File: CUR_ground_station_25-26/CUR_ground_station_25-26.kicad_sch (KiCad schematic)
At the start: 0 parts

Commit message: added sheets and mcu
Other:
- added sheet MCU (MCU.kicad_sch)
- added sheet Power (Power.kicad_sch)
- added sheet Telemetry (Telemetry.kicad_sch)
- added sheet User Interface (Peripherals.kicad_sch)
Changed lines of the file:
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@@
 	(generator_version "9.0")
 	(paper "A4")
+	(sheet
+		(at 77.47 91.44)
+		(size 39.37 17.78)
+		(exclude_from_sim no)
+		(in_bom yes)
+		(on_board yes)
+		(dnp no)
+		(fields_autoplaced yes)
+		(stroke
+			(width 0.1524)
+			(type solid)
+		)
+		(fill
+			(color 0 0 0 0.0000)
+		)
+		(property "Sheetname" "User Interface"
+			(at 77.47 90.7284 0)
+			(effects
+				(font
+					(size 1.27 1.27)
+				)
+				(justify left bottom)
+			)
+		)
+		(property "Sheetfile" "Peripherals.kicad_sch"
+			(at 77.47 109.8046 0)
+			(effects
+				(font
+					(size 1.27 1.27)
+				)
+				(justify left top)
+			)
+		)
+		(instances
+			(project "CUR_ground_station_25-26"
+				(path "/b6f682bd-f29b-4650-adb4-b230be0368ad"
+					(page "5")
+				)
+			)
+		)
+	)
+	(sheet
+		(at 167.64 109.22)
+		(size 43.18 17.78)
+		(exclude_from_sim no)
+		(in_bom yes)
+		(on_board yes)
+		(dnp no)
+		(fields_autoplaced yes)
+		(stroke
+			(width 0.1524)
+			(type solid)
+		)
+		(fill
+			(color 0 0 0 0.0000)
+		)
+		(property "Sheetname" "Power"
+			(at 167.64 108.5084 0)
+			(effects
+				(font
+					(size 1.27 1.27)
+				)
+				(justify left bottom)
+			)
+		)
+		(property "Sheetfile" "Power.kicad_sch"
+			(at 167.64 127.5846 0)
+			(effects
+				(font
+					(size 1.27 1.27)
+				)
+				(justify left top)
+			)
+		)
+		(instances
+			(project "CUR_ground_station_25-26"
+				(path "/b6f682bd-f29b-4650-adb4-b230be0368ad"
+					(page "4")
+				)
+			)
+		)
+	)
+	(sheet
+		(at 124.46 66.04)
+		(size 36.83 78.74)
+		(exclude_from_sim no)
+		(in_bom yes)
+		(on_board yes)
+		(dnp no)
+		(fields_autoplaced yes)
+		(stroke
+			(width 0.1524)
+			(type solid)
+		)
+		(fill
+			(color 0 0 0 0.0000)
+		)
+		(property "Sheetname" "MCU"
+			(at 124.46 65.3284 0)
+			(effects
+				(font
+					(size 1.27 1.27)
+				)
+				(justify left bottom)
+			)
+		)
+		(property "Sheetfile" "MCU.kicad_sch"
+			(at 124.46 145.3646 0)
+			(effects
+				(font
+					(size 1.27 1.27)
+				)
+				(justify left top)
+			)
+		)
+		(instances
+			(project "CUR_ground_station_25-26"
+				(path "/b6f682bd-f29b-4650-adb4-b230be0368ad"
+					(page "2")
+				)
+			)
+		)
+	)
+	(sheet
+		(at 167.64 76.2)
+		(size 43.18 22.86)
+		(exclude_from_sim no)
+		(in_bom yes)
+		(on_board yes)
+		(dnp no)
+		(fields_autoplaced yes)
+		(stroke
+			(width 0.1524)
+			(type solid)
+		)
+		(fill
+			(color 0 0 0 0.0000)
+		)
+		(property "Sheetname" "Telemetry"
+			(at 167.64 75.4884 0)
+			(effects
+				(font
+					(size 1.27 1.27)
+				)
+				(justify left bottom)
+			)
+		)
+		(property "Sheetfile" "Telemetry.kicad_sch"
+			(at 167.64 99.6446 0)
+			(effects
+				(font
+					(size 1.27 1.27)
+				)
+				(justify left top)
+			)
+		)
+		(instances
+			(project "CUR_ground_station_25-26"
+				(path "/b6f682bd-f29b-4650-adb4-b230be0368ad"
+					(page "3")
+				)
+			)
+		)
+	)
 	(sheet_instances
 		(path "/"

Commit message: added user stuff
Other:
- sheet MCU ports: added BTN_1, BUZZER, LED_1_B, LED_1_G, LED_1_R, LED_2_B, LED_2_G, LED_2_R, LED_3_B, LED_3_G, LED_3_R; removed none
- sheet User Interface ports: added BTN_1, Buzzer, LED_1_B, LED_1_G, LED_1_R, LED_2_B, LED_2_G, LED_2_R, LED_3_B, LED_3_G, LED_3_R; removed none

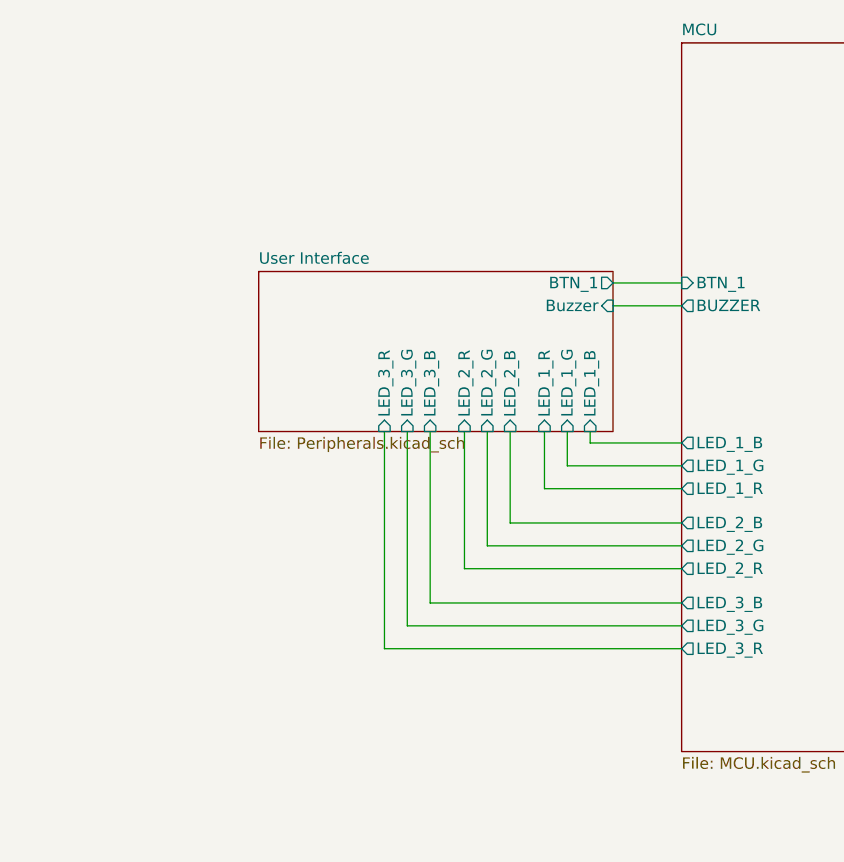
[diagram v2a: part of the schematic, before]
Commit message: Add some required MCU components
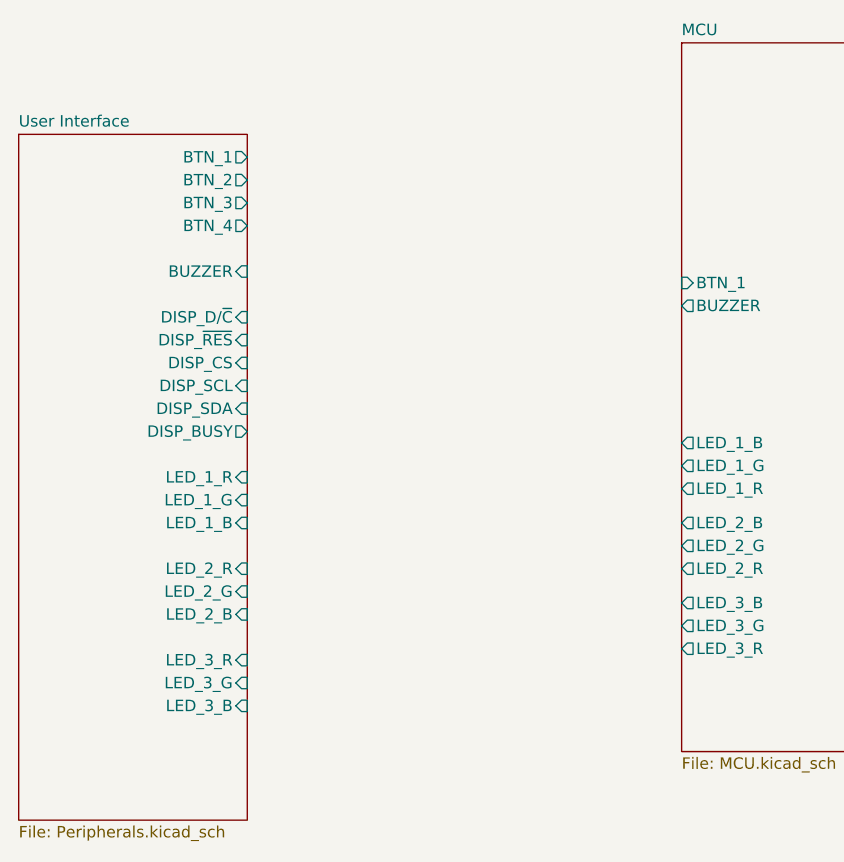
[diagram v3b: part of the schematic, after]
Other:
- sheet User Interface ports: added BTN_2, BTN_3, BTN_4, BUZZER, DISP_BUSY, DISP_CS, DISP_D/~{C}, DISP_SCL, DISP_SDA, DISP_~{RES}; removed Buzzer

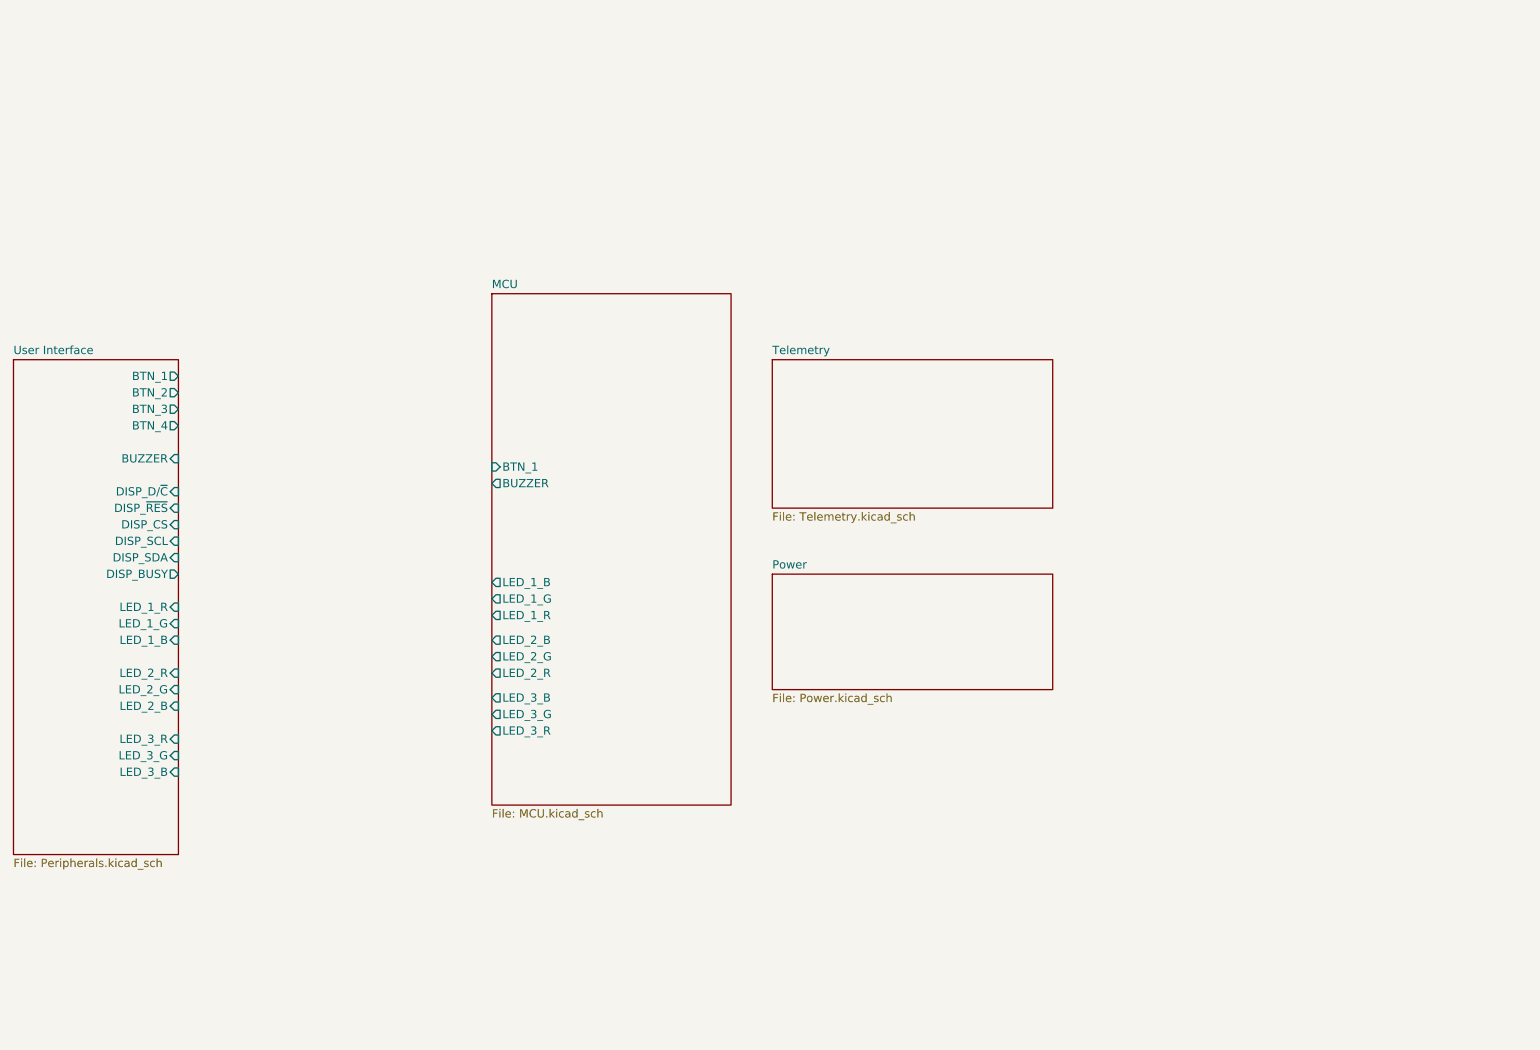
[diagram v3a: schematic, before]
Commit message: Sync sheet pins
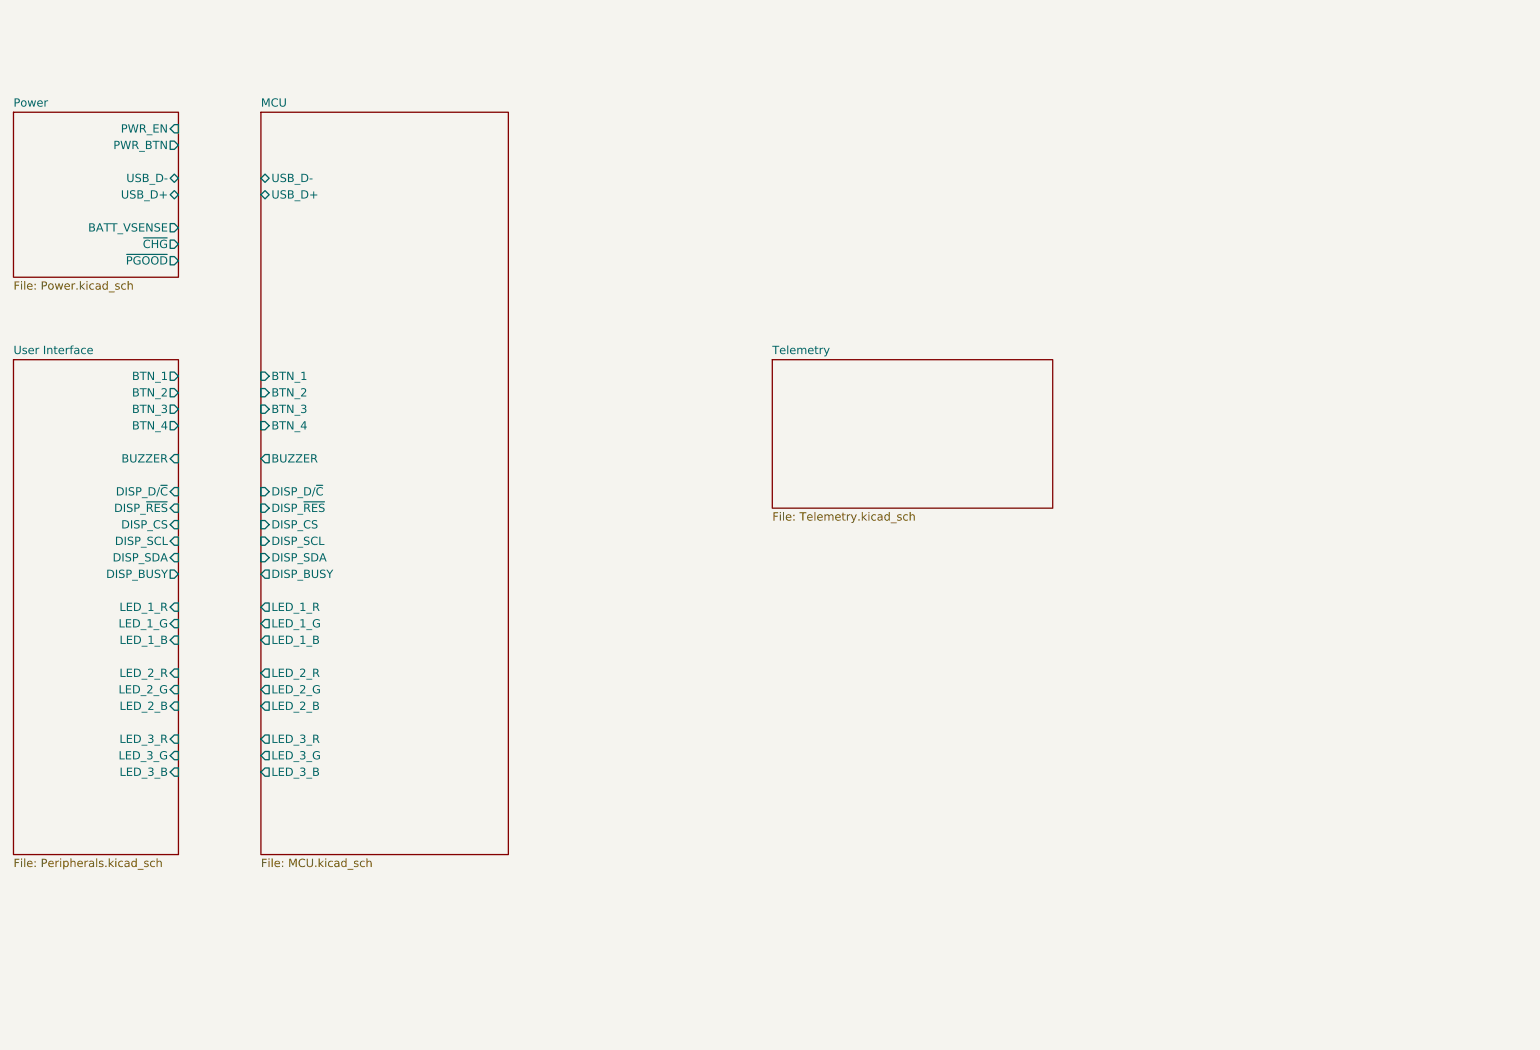
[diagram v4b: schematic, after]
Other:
- sheet MCU ports: added BTN_2, BTN_3, BTN_4, DISP_BUSY, DISP_CS, DISP_D/~{C}, DISP_SCL, DISP_SDA, DISP_~{RES}, USB_D+, USB_D-; removed none
- sheet Power ports: added BATT_VSENSE, PWR_BTN, PWR_EN, USB_D+, USB_D-, ~{CHG}, ~{PGOOD}; removed none
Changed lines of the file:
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@@
 	)
 	(sheet
-		(at 167.64 109.22)
-		(size 43.18 17.78)
+		(at 50.8 38.1)
+		(size 25.4 25.4)
 		(exclude_from_sim no)
 		(in_bom yes)
@@
 		)
 		(property "Sheetname" "Power"
-			(at 167.64 108.5084 0)
+			(at 50.8 37.3884 0)
 			(effects
 				(font
@@
 		)
 		(property "Sheetfile" "Power.kicad_sch"
-			(at 167.64 127.5846 0)
+			(at 50.8 64.0846 0)
 			(effects
 				(font
@@
 				)
 				(justify left top)
+			)
+		)
+		(pin "~{PGOOD}" output
+			(at 76.2 60.96 0)
+			(effects
+				(font
+					(size 1.27 1.27)
+				)
+				(justify right)
+			)
+		)
+		(pin "~{CHG}" output
+			(at 76.2 58.42 0)
+			(effects
+				(font
+					(size 1.27 1.27)
+				)
+				(justify right)
+			)
+		)
+		(pin "BATT_VSENSE" output
+			(at 76.2 55.88 0)
+			(effects
+				(font
+					(size 1.27 1.27)
+				)
+				(justify right)
+			)
+		)
+		(pin "PWR_EN" input
+			(at 76.2 40.64 0)
+			(effects
+				(font
+					(size 1.27 1.27)
+				)
+				(justify right)
+			)
+		)
+		(pin "USB_D-" bidirectional
+			(at 76.2 48.26 0)
+			(effects
+				(font
+					(size 1.27 1.27)
+				)
+				(justify right)
+			)
+		)
+		(pin "USB_D+" bidirectional
+			(at 76.2 50.8 0)
+			(effects
+				(font
+					(size 1.27 1.27)
+				)
+				(justify right)
+			)
+		)
+		(pin "PWR_BTN" output
+			(at 76.2 43.18 0)
+			(effects
+				(font
+					(size 1.27 1.27)
+				)
+				(justify right)
 			)
 		)
@@
 	)
 	(sheet
-		(at 124.46 66.04)
-		(size 36.83 78.74)
+		(at 88.9 38.1)
+		(size 38.1 114.3)
 		(exclude_from_sim no)
 		(in_bom yes)
@@
 		)
 		(property "Sheetname" "MCU"
-			(at 124.46 65.3284 0)
+			(at 88.9 37.3884 0)
 			(effects
 				(font
@@
 		)
 		(property "Sheetfile" "MCU.kicad_sch"
-			(at 124.46 145.3646 0)
+			(at 88.9 152.9846 0)
 			(effects
 				(font
@@
 		)
 		(pin "BTN_1" input
-			(at 124.46 92.71 180)
+			(at 88.9 78.74 180)
 			(effects
 				(font
@@
 		)
 		(pin "BUZZER" output
-			(at 124.46 95.25 180)
+			(at 88.9 91.44 180)
 			(effects
 				(font
@@
 		)
 		(pin "LED_1_B" output
-			(at 124.46 110.49 180)
+			(at 88.9 119.38 180)
 			(effects
 				(font
@@
 		)
 		(pin "LED_1_G" output
-			(at 124.46 113.03 180)
+			(at 88.9 116.84 180)
 			(effects
 				(font
@@
 		)
 		(pin "LED_1_R" output
-			(at 124.46 115.57 180)
+			(at 88.9 114.3 180)
 			(effects
 				(font
@@
 		)
 		(pin "LED_2_B" output
-			(at 124.46 119.38 180)
+			(at 88.9 129.54 180)
 			(effects
 				(font
@@
 		)
 		(pin "LED_2_G" output
-			(at 124.46 121.92 180)
+			(at 88.9 127 180)
 			(effects
 				(font
@@
 		)
 		(pin "LED_2_R" output
-			(at 124.46 124.46 180)
+			(at 88.9 124.46 180)
 			(effects
 				(font
@@
 		)
 		(pin "LED_3_B" output
-			(at 124.46 128.27 180)
+			(at 88.9 139.7 180)
 			(effects
 				(font
@@
 		)
 		(pin "LED_3_G" output
-			(at 124.46 130.81 180)
+			(at 88.9 137.16 180)
 			(effects
 				(font
@@
 		)
 		(pin "LED_3_R" output
-			(at 124.46 133.35 180)
-			(effects
-				(font
+			(at 88.9 134.62 180)
+			(effects
+				(font
+					(size 1.27 1.27)
+				)
+				(justify left)
+			)
+		)
+		(pin "BTN_4" input
+			(at 88.9 86.36 180)
+			(effects
+				(font
+					(size 1.27 1.27)
+				)
+				(justify left)
+			)
+		)
+		(pin "USB_D-" bidirectional
+			(at 88.9 48.26 180)
+			(effects
+				(font
+					(size 1.27 1.27)
+				)
+				(justify left)
+			)
+		)
+		(pin "DISP_D/~{C}" input
+			(at 88.9 96.52 180)
+			(effects
+				(font
+					(size 1.27 1.27)
+				)
+				(justify left)
+			)
+		)
+		(pin "DISP_CS" input
+			(at 88.9 101.6 180)
+			(effects
+				(font
+					(size 1.27 1.27)
+				)
+				(justify left)
+			)
+		)
+		(pin "DISP_SDA" input
+			(at 88.9 106.68 180)
+			(effects
+				(font
+					(size 1.27 1.27)
+				)
+				(justify left)
+			)
+		)
+		(pin "DISP_~{RES}" input
+			(at 88.9 99.06 180)
+			(effects
+				(font
+					(size 1.27 1.27)
+				)
+				(justify left)
+			)
+		)
+		(pin "DISP_BUSY" output
+			(at 88.9 109.22 180)
+			(effects
+				(font
+					(size 1.27 1.27)
+				)
+				(justify left)
+			)
+		)
+		(pin "DISP_SCL" input
+			(at 88.9 104.14 180)
+			(effects
+				(font
+					(size 1.27 1.27)
+				)
+				(justify left)
+			)
+		)
+		(pin "BTN_2" input
+			(at 88.9 81.28 180)
+			(effects
+				(font
+					(size 1.27 1.27)
+				)
+				(justify left)
+			)
+		)
+		(pin "BTN_3" input
+			(at 88.9 83.82 180)
+			(effects
+				(font
+					(size 1.27 1.27)
+				)
+				(justify left)
+			)
+		)
+		(pin "USB_D+" bidirectional
+			(at 88.9 50.8 180)
+			(effects
+				(font

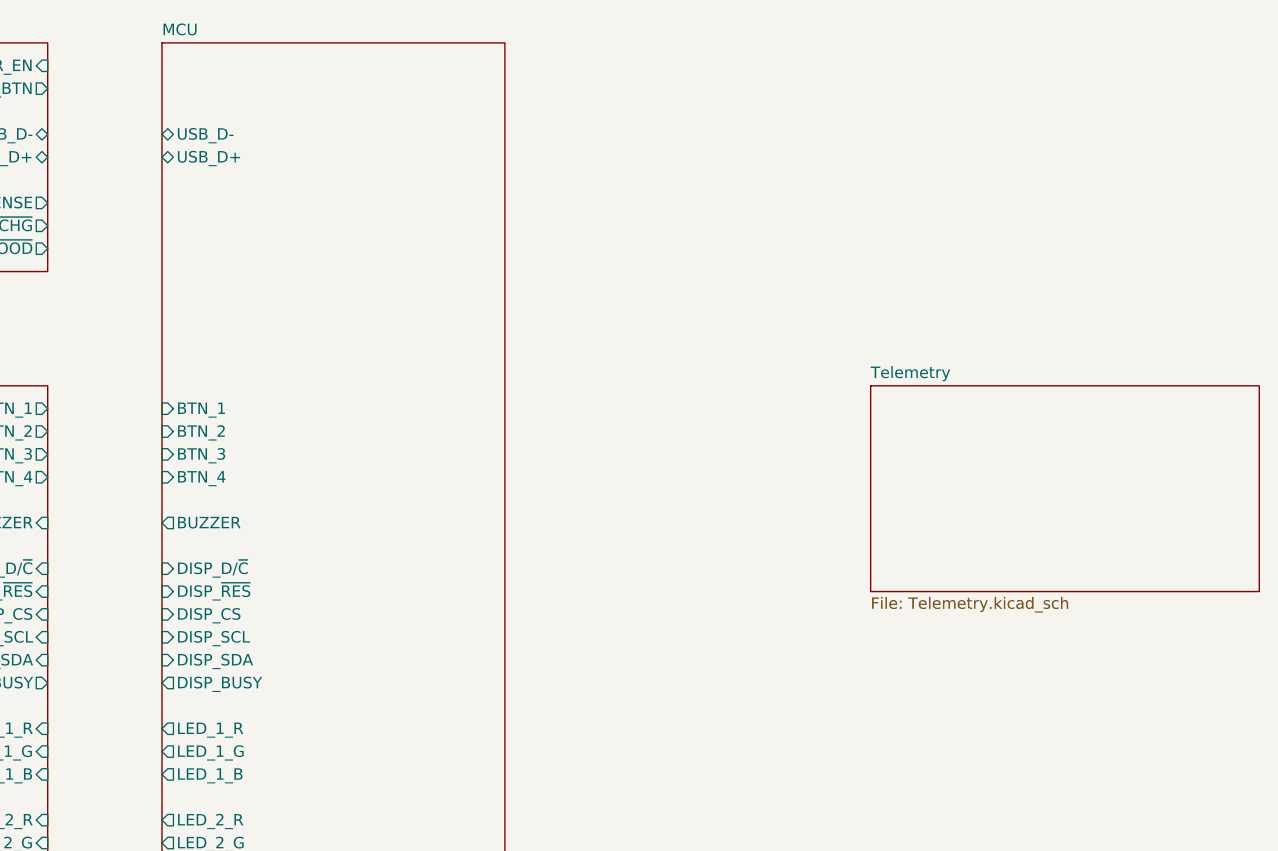
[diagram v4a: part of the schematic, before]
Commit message: sync sheet pins
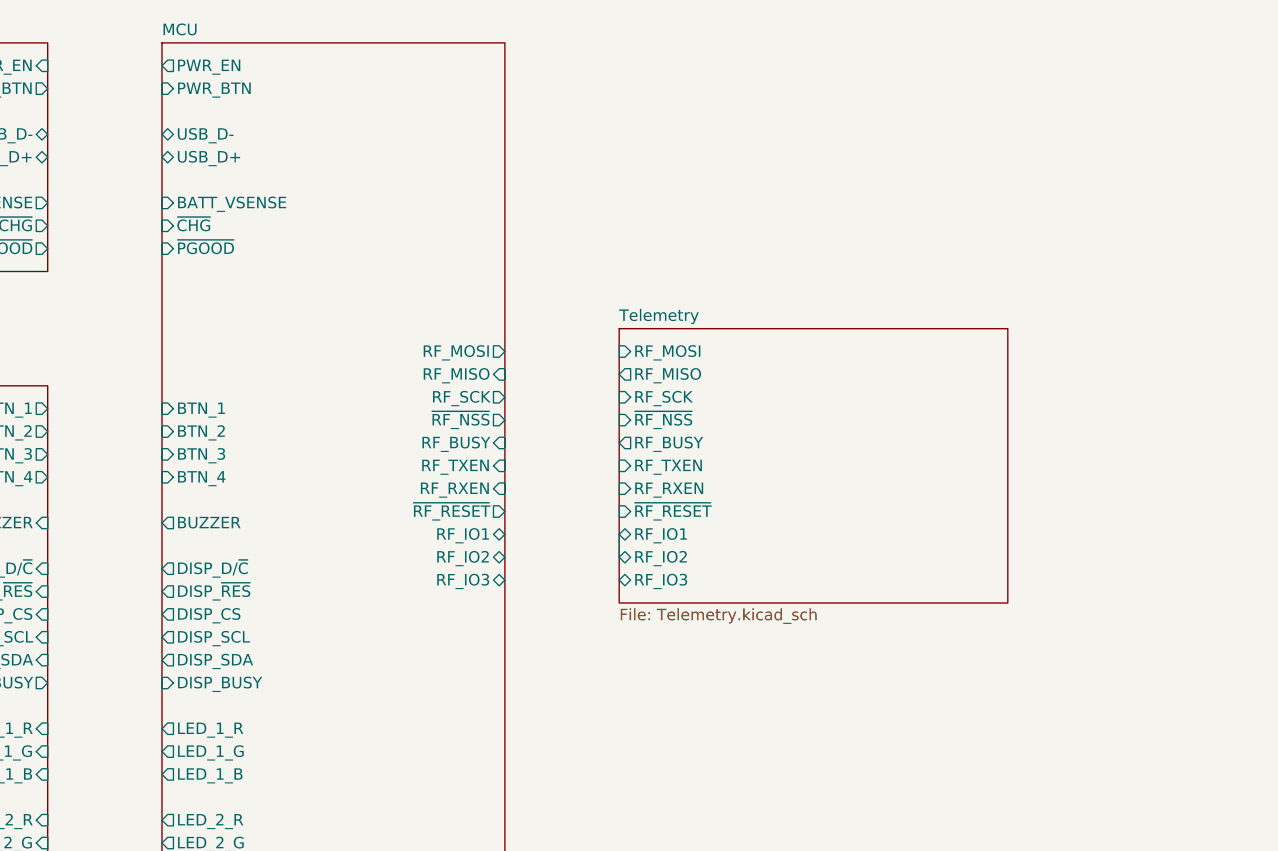
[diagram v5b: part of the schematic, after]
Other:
- sheet MCU ports: added BATT_VSENSE, DISP_D/~{C}, PWR_BTN, PWR_EN, RF_BUSY, RF_IO1, RF_IO2, RF_IO3, RF_MISO, RF_MOSI, RF_RXEN, RF_SCK, RF_TXEN, ~{CHG}, ~{PGOOD}, ~{RF_NSS}, ~{RF_RESET}; removed DISP_D/~{C}
- sheet Telemetry ports: added RF_BUSY, RF_IO1, RF_IO2, RF_IO3, RF_MISO, RF_MOSI, RF_RXEN, RF_SCK, RF_TXEN, ~{RF_NSS}, ~{RF_RESET}; removed none
